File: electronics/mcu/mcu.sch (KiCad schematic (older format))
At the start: 11 parts

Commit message: add footprints
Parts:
- removed X?: 8MHz, symbol CRYSTAL
- added X1: 8MHz, symbol CRYSTAL_S
- C1, C3, C4: renamed from C?; footprint (none) -> Capacitors_ThroughHole:Capacitor7.5MMDiscRM5
- C2: renamed from C?; footprint (none) -> Capacitors_Elko_ThroughHole:Elko_vert_20x10mm_RM5
- IC1: renamed from IC?; footprint SO20 -> SMD_Packages:SO-20-L
- P1: renamed from P?; footprint (none) -> Pin_Headers:Pin_Header_Straight_1x02
- P2: renamed from P?; footprint (none) -> Pin_Headers:Pin_Header_Straight_1x06
- P3: renamed from P?; footprint (none) -> Pin_Headers:Pin_Header_Straight_1x05
- P4: renamed from P?; footprint (none) -> Pin_Headers:Pin_Header_Straight_2x07
- R1: renamed from R?; footprint (none) -> Resistors_ThroughHole:Resistor_Horizontal_RM10mm
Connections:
- wire segments 46 -> 47
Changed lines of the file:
@@
 LIBS:contrib
 LIBS:valves
+LIBS:crystal_s
 LIBS:mcu-cache
 EELAYER 25 0
@@
 $EndDescr
 $Comp
-L ATTINY2313-S IC?
+L ATTINY2313-S IC1
 U 1 1 560C33C8
 P 4900 3300
-F 0 "IC?" H 3950 4300 40  0000 C CNN
+F 0 "IC1" H 3950 4300 40  0000 C CNN
 F 1 "ATTINY2313-S" H 5650 2400 40  0000 C CNN
-F 2 "SO20" H 4900 3300 35  0000 C CIN
+F 2 "SMD_Packages:SO-20-L" H 4900 3300 35  0000 C CIN
 F 3 "" H 4900 3300 60  0000 C CNN
 	1    4900 3300
@@
 $EndComp
 $Comp
-L CONN_01X05 P?
+L CONN_01X05 P3
 U 1 1 560C3E46
 P 7050 3100
-F 0 "P?" H 7050 3400 50  0000 C CNN
+F 0 "P3" H 7050 3400 50  0000 C CNN
 F 1 "SPI" V 7150 3100 50  0000 C CNN
-F 2 "" H 7050 3100 60  0000 C CNN
+F 2 "Pin_Headers:Pin_Header_Straight_1x05" H 7050 3100 60  0001 C CNN
 F 3 "" H 7050 3100 60  0000 C CNN
 	1    7050 3100
@@
 $EndComp
 $Comp
-L GND #PWR?
+L GND #PWR01
 U 1 1 560C404C
 P 6800 3300
-F 0 "#PWR?" H 6800 3050 60  0001 C CNN
+F 0 "#PWR01" H 6800 3050 60  0001 C CNN
 F 1 "GND" H 6800 3150 60  0001 C CNN
 F 2 "" H 6800 3300 60  0000 C CNN
@@
 $EndComp
 $Comp
-L CONN_01X06 P?
+L CONN_01X06 P2
 U 1 1 560C60F9
 P 6400 2650
-F 0 "P?" H 6400 3000 50  0000 C CNN
+F 0 "P2" H 6400 3000 50  0000 C CNN
 F 1 "CONTROL" V 6500 2650 50  0000 C CNN
-F 2 "" H 6400 2650 60  0000 C CNN
+F 2 "Pin_Headers:Pin_Header_Straight_1x06" H 6400 2650 60  0001 C CNN
 F 3 "" H 6400 2650 60  0000 C CNN
 	1    6400 2650
@@
 $EndComp
 $Comp
-L GND #PWR?
+L GND #PWR02
 U 1 1 560C61BB
 P 6150 2400
-F 0 "#PWR?" H 6150 2150 60  0001 C CNN
+F 0 "#PWR02" H 6150 2150 60  0001 C CNN
 F 1 "GND" H 6150 2250 60  0001 C CNN
 F 2 "" H 6150 2400 60  0000 C CNN
@@
 $EndComp
 $Comp
-L CONN_02X07 P?
+L CONN_02X07 P4
 U 1 1 560C626E
 P 6400 3700
-F 0 "P?" H 6400 4100 50  0000 C CNN
+F 0 "P4" H 6400 4100 50  0000 C CNN
 F 1 "EXTRA" V 6400 3700 50  0000 C CNN
-F 2 "" H 6400 2500 60  0000 C CNN
+F 2 "Pin_Headers:Pin_Header_Straight_2x07" H 6400 2500 60  0001 C CNN
 F 3 "" H 6400 2500 60  0000 C CNN
 	1    6400 3700
@@
 $EndComp
 $Comp
-L GND #PWR?
+L GND #PWR03
 U 1 1 560C6457
 P 6750 4100
-F 0 "#PWR?" H 6750 3850 60  0001 C CNN
+F 0 "#PWR03" H 6750 3850 60  0001 C CNN
 F 1 "GND" H 6750 3950 60  0001 C CNN
 F 2 "" H 6750 4100 60  0000 C CNN
@@
 $EndComp
 $Comp
-L GND #PWR?
+L GND #PWR04
 U 1 1 560C656B
 P 4900 4400
-F 0 "#PWR?" H 4900 4150 60  0001 C CNN
+F 0 "#PWR04" H 4900 4150 60  0001 C CNN
 F 1 "GND" H 4900 4250 60  0001 C CNN
 F 2 "" H 4900 4400 60  0000 C CNN
@@
 $EndComp
 $Comp
-L C C?
+L C C4
 U 1 1 560C6654
 P 3650 3400
-F 0 "C?" H 3650 3500 40  0000 L CNN
+F 0 "C4" H 3650 3500 40  0000 L CNN
 F 1 "22p" H 3656 3315 40  0000 L CNN
-F 2 "" H 3688 3250 30  0000 C CNN
+F 2 "Capacitors_ThroughHole:Capacitor7.5MMDiscRM5" H 3688 3250 30  0001 C CNN
 F 3 "" H 3650 3400 60  0000 C CNN
 	1    3650 3400
@@
 $EndComp
 $Comp
-L C C?
+L C C3
 U 1 1 560C6706
 P 2850 3400
-F 0 "C?" H 2850 3500 40  0000 L CNN
+F 0 "C3" H 2850 3500 40  0000 L CNN
 F 1 "22p" H 2856 3315 40  0000 L CNN
-F 2 "" H 2888 3250 30  0000 C CNN
+F 2 "Capacitors_ThroughHole:Capacitor7.5MMDiscRM5" H 2888 3250 30  0001 C CNN
 F 3 "" H 2850 3400 60  0000 C CNN
 	1    2850 3400
 	1    0    0    -1
 $EndComp
-$Comp
-L CRYSTAL X?
-U 1 1 560C6750
-P 3250 3000
-F 0 "X?" H 3250 3150 60  0000 C CNN
-F 1 "8MHz" H 3250 2850 60  0000 C CNN
-F 2 "" H 3250 3000 60  0000 C CNN
-F 3 "" H 3250 3000 60  0000 C CNN
-	1    3250 3000
-	1    0    0    -1
-$EndComp
 Wire Wire Line
 	6850 3200 6050 3200
@@
 Connection ~ 2850 3000
 $Comp
-L GND #PWR?
+L GND #PWR05
 U 1 1 560C6999
 P 3650 3700
-F 0 "#PWR?" H 3650 3450 60  0001 C CNN
+F 0 "#PWR05" H 3650 3450 60  0001 C CNN
 F 1 "GND" H 3650 3550 60  0001 C CNN
 F 2 "" H 3650 3700 60  0000 C CNN
@@
 	3650 3700 3650 3600
 $Comp
-L GND #PWR?
+L GND #PWR06
 U 1 1 560C69EE
 P 2850 3700
-F 0 "#PWR?" H 2850 3450 60  0001 C CNN
+F 0 "#PWR06" H 2850 3450 60  0001 C CNN
 F 1 "GND" H 2850 3550 60  0001 C CNN
 F 2 "" H 2850 3700 60  0000 C CNN
@@
 	2850 3700 2850 3600
 $Comp
-L R R?
+L R R1
 U 1 1 560C6A62
 P 3600 1750
-F 0 "R?" H 3700 1750 40  0000 C CNN
+F 0 "R1" H 3700 1750 40  0000 C CNN
 F 1 "10k" H 3700 1550 40  0000 C CNN
-F 2 "" V 3530 1750 30  0000 C CNN
+F 2 "Resistors_ThroughHole:Resistor_Horizontal_RM10mm" V 3530 1750 30  0001 C CNN
 F 3 "" H 3600 1750 30  0000 C CNN
 	1    3600 1750
@@
 Connection ~ 3600 2100
 $Comp
-L CP2 C?
+L CP2 C2
 U 1 1 560C6C7E
 P 5450 1700
-F 0 "C?" H 5450 1800 40  0000 L CNN
+F 0 "C2" H 5450 1800 40  0000 L CNN
 F 1 "22u" H 5456 1615 40  0000 L CNN
-F 2 "" H 5488 1550 30  0000 C CNN
+F 2 "Capacitors_Elko_ThroughHole:Elko_vert_20x10mm_RM5" H 5488 1550 30  0001 C CNN
 F 3 "" H 5450 1700 60  0000 C CNN
 	1    5450 1700
@@
 $EndComp
 $Comp
-L C C?
+L C C1
 U 1 1 560C6D7B
 P 5150 1700
-F 0 "C?" H 5150 1800 40  0000 L CNN
+F 0 "C1" H 5150 1800 40  0000 L CNN
 F 1 "100n" H 5156 1615 40  0000 L CNN
-F 2 "" H 5188 1550 30  0000 C CNN
+F 2 "Capacitors_ThroughHole:Capacitor7.5MMDiscRM5" H 5188 1550 30  0001 C CNN
 F 3 "" H 5150 1700 60  0000 C CNN
 	1    5150 1700
@@
 $EndComp
 $Comp
-L CONN_01X02 P?
+L CONN_01X02 P1
 U 1 1 560C6E13
 P 6050 1450
-F 0 "P?" H 6050 1600 50  0000 C CNN
+F 0 "P1" H 6050 1600 50  0000 C CNN
 F 1 "3.3v" V 6150 1450 50  0000 C CNN
-F 2 "" H 6050 1450 60  0000 C CNN
+F 2 "Pin_Headers:Pin_Header_Straight_1x02" H 6050 1450 60  0001 C CNN
 F 3 "" H 6050 1450 60  0000 C CNN
 	1    6050 1450
@@
 Connection ~ 5450 1400
 $Comp
-L GND #PWR?
+L GND #PWR07
 U 1 1 560C6FBB
 P 5150 1950
-F 0 "#PWR?" H 5150 1700 60  0001 C CNN
+F 0 "#PWR07" H 5150 1700 60  0001 C CNN
 F 1 "GND" H 5150 1800 60  0001 C CNN
 F 2 "" H 5150 1950 60  0000 C CNN
@@
 	5150 1950 5150 1900
 $Comp
-L GND #PWR?
+L GND #PWR08
 U 1 1 560C7062
 P 5450 1950
-F 0 "#PWR?" H 5450 1700 60  0001 C CNN
+F 0 "#PWR08" H 5450 1700 60  0001 C CNN
 F 1 "GND" H 5450 1800 60  0001 C CNN
 F 2 "" H 5450 1950 60  0000 C CNN
@@
 	5450 1950 5450 1900
 $Comp
-L GND #PWR?
+L GND #PWR09
 U 1 1 560C70E9
 P 5800 1500
-F 0 "#PWR?" H 5800 1250 60  0001 C CNN
+F 0 "#PWR09" H 5800 1250 60  0001 C CNN
 F 1 "GND" H 5800 1350 60  0001 C CNN
 F 2 "" H 5800 1500 60  0000 C CNN
@@
 Wire Wire Line
 	5850 1500 5800 1500
+$Comp
+L CRYSTAL_S X1
+U 1 1 560C845C
+P 3250 3000
+F 0 "X1" H 3250 3150 60  0000 C CNN
+F 1 "8MHz" H 3400 2800 60  0000 C CNN
+F 2 "" H 3250 3000 60  0000 C CNN
+F 3 "" H 3250 3000 60  0000 C CNN
+	1    3250 3000
+	1    0    0    -1
+$EndComp
+$Comp
+L GND #PWR?
+U 1 1 560C8672
+P 3250 3350
+F 0 "#PWR?" H 3250 3100 60  0001 C CNN
+F 1 "GND" H 3250 3200 60  0001 C CNN
+F 2 "" H 3250 3350 60  0000 C CNN
+F 3 "" H 3250 3350 60  0000 C CNN
+	1    3250 3350
+	1    0    0    -1
+$EndComp
+Wire Wire Line
+	3250 3350 3250 3250
 $EndSCHEMATC

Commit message: some minor tweaks
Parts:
- X1: footprint (none) -> QMONTRE_P:QMONTRE_P
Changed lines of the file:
@@
 F 0 "X1" H 3250 3150 60  0000 C CNN
 F 1 "8MHz" H 3400 2800 60  0000 C CNN
-F 2 "" H 3250 3000 60  0000 C CNN
+F 2 "QMONTRE_P:QMONTRE_P" H 3250 3000 60  0001 C CNN
 F 3 "" H 3250 3000 60  0000 C CNN
 	1    3250 3000
@@
 $EndComp
 $Comp
-L GND #PWR?
+L GND #PWR010
 U 1 1 560C8672
 P 3250 3350
-F 0 "#PWR?" H 3250 3100 60  0001 C CNN
+F 0 "#PWR010" H 3250 3100 60  0001 C CNN
 F 1 "GND" H 3250 3200 60  0001 C CNN
 F 2 "" H 3250 3350 60  0000 C CNN

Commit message: finish the pcb
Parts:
- removed P4: EXTRA, Pin_Headers:Pin_Header_Straight_2x07, symbol CONN_02X07
- added P4: EXTRA, symbol CONN_02X06
- X1: footprint QMONTRE_P:QMONTRE_P -> HC-49V_S:HC-49V_S
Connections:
- net GND: now also P4.10 (P10), P4.12 (P12), P4.2 (P2), P4.4 (P4), P4.6 (P6), P4.8 (P8)
- net at IC1.2 ((RXD)PD0): now also P4.1 (P1)
- net at IC1.3 ((TXD)PD1): now also P4.3 (P3)
- net at IC1.6 ((CKOUT/XCK/INT0)PD2): now also P4.5 (P5)
- net at IC1.7 ((INT1)PD3): now also P4.7 (P7)
- net at IC1.8 ((T0)PD4): now also P4.9 (P9)
- net at IC1.9 ((OC0B/T1)PD5): now also P4.11 (P11)
- no-connect marks 0 -> 1
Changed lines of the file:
@@
 $EndComp
 $Comp
-L GND #PWR01
+L GND #PWR5
 U 1 1 560C404C
 P 6800 3300
-F 0 "#PWR01" H 6800 3050 60  0001 C CNN
+F 0 "#PWR5" H 6800 3050 60  0001 C CNN
 F 1 "GND" H 6800 3150 60  0001 C CNN
 F 2 "" H 6800 3300 60  0000 C CNN
@@
 $EndComp
 $Comp
-L GND #PWR02
+L GND #PWR4
 U 1 1 560C61BB
 P 6150 2400
-F 0 "#PWR02" H 6150 2150 60  0001 C CNN
+F 0 "#PWR4" H 6150 2150 60  0001 C CNN
 F 1 "GND" H 6150 2250 60  0001 C CNN
 F 2 "" H 6150 2400 60  0000 C CNN
@@
 $EndComp
 $Comp
-L CONN_02X07 P4
-U 1 1 560C626E
-P 6400 3700
-F 0 "P4" H 6400 4100 50  0000 C CNN
-F 1 "EXTRA" V 6400 3700 50  0000 C CNN
-F 2 "Pin_Headers:Pin_Header_Straight_2x07" H 6400 2500 60  0001 C CNN
-F 3 "" H 6400 2500 60  0000 C CNN
-	1    6400 3700
-	1    0    0    -1
-$EndComp
-$Comp
-L GND #PWR03
+L GND #PWR9
 U 1 1 560C6457
 P 6750 4100
-F 0 "#PWR03" H 6750 3850 60  0001 C CNN
+F 0 "#PWR9" H 6750 3850 60  0001 C CNN
 F 1 "GND" H 6750 3950 60  0001 C CNN
 F 2 "" H 6750 4100 60  0000 C CNN
@@
 $EndComp
 $Comp
-L GND #PWR04
+L GND #PWR10
 U 1 1 560C656B
 P 4900 4400
-F 0 "#PWR04" H 4900 4150 60  0001 C CNN
+F 0 "#PWR10" H 4900 4150 60  0001 C CNN
 F 1 "GND" H 4900 4250 60  0001 C CNN
 F 2 "" H 4900 4400 60  0000 C CNN
@@
 	6050 3900 6150 3900
 Wire Wire Line
-	6150 4000 6050 4000
-Wire Wire Line
 	6750 4100 6750 3400
 Wire Wire Line
@@
 Connection ~ 6750 3900
 Wire Wire Line
-	6650 4000 6750 4000
-Connection ~ 6750 4000
-Wire Wire Line
 	4900 4400 4900 4300
 Wire Wire Line
@@
 Connection ~ 2850 3000
 $Comp
-L GND #PWR05
+L GND #PWR8
 U 1 1 560C6999
 P 3650 3700
-F 0 "#PWR05" H 3650 3450 60  0001 C CNN
+F 0 "#PWR8" H 3650 3450 60  0001 C CNN
 F 1 "GND" H 3650 3550 60  0001 C CNN
 F 2 "" H 3650 3700 60  0000 C CNN
@@
 	3650 3700 3650 3600
 $Comp
-L GND #PWR06
+L GND #PWR7
 U 1 1 560C69EE
 P 2850 3700
-F 0 "#PWR06" H 2850 3450 60  0001 C CNN
+F 0 "#PWR7" H 2850 3450 60  0001 C CNN
 F 1 "GND" H 2850 3550 60  0001 C CNN
 F 2 "" H 2850 3700 60  0000 C CNN
@@
 Connection ~ 5450 1400
 $Comp
-L GND #PWR07
+L GND #PWR2
 U 1 1 560C6FBB
 P 5150 1950
-F 0 "#PWR07" H 5150 1700 60  0001 C CNN
+F 0 "#PWR2" H 5150 1700 60  0001 C CNN
 F 1 "GND" H 5150 1800 60  0001 C CNN
 F 2 "" H 5150 1950 60  0000 C CNN
@@
 	5150 1950 5150 1900
 $Comp
-L GND #PWR08
+L GND #PWR3
 U 1 1 560C7062
 P 5450 1950
-F 0 "#PWR08" H 5450 1700 60  0001 C CNN
+F 0 "#PWR3" H 5450 1700 60  0001 C CNN
 F 1 "GND" H 5450 1800 60  0001 C CNN
 F 2 "" H 5450 1950 60  0000 C CNN
@@
 	5450 1950 5450 1900
 $Comp
-L GND #PWR09
+L GND #PWR1
 U 1 1 560C70E9
 P 5800 1500
-F 0 "#PWR09" H 5800 1250 60  0001 C CNN
+F 0 "#PWR1" H 5800 1250 60  0001 C CNN
 F 1 "GND" H 5800 1350 60  0001 C CNN
 F 2 "" H 5800 1500 60  0000 C CNN
@@
 F 0 "X1" H 3250 3150 60  0000 C CNN
 F 1 "8MHz" H 3400 2800 60  0000 C CNN
-F 2 "QMONTRE_P:QMONTRE_P" H 3250 3000 60  0001 C CNN
+F 2 "HC-49V_S:HC-49V_S" H 3250 3000 60  0001 C CNN
 F 3 "" H 3250 3000 60  0000 C CNN
 	1    3250 3000
@@
 $EndComp
 $Comp
-L GND #PWR010
+L GND #PWR6
 U 1 1 560C8672
 P 3250 3350
-F 0 "#PWR010" H 3250 3100 60  0001 C CNN
+F 0 "#PWR6" H 3250 3100 60  0001 C CNN
 F 1 "GND" H 3250 3200 60  0001 C CNN
 F 2 "" H 3250 3350 60  0000 C CNN
@@
 Wire Wire Line
 	3250 3350 3250 3250
+$Comp
+L CONN_02X06 P4
+U 1 1 561BC094
+P 6400 3650
+F 0 "P4" H 6400 4000 50  0000 C CNN
+F 1 "EXTRA" V 6400 3650 50  0000 C CNN
+F 2 "" H 6400 2450 60  0000 C CNN
+F 3 "" H 6400 2450 60  0000 C CNN
+	1    6400 3650
+	1    0    0    -1
+$EndComp
+NoConn ~ 6050 4000
 $EndSCHEMATC

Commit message: finish the PCB
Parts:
- P4: footprint (none) -> Pin_Headers:Pin_Header_Straight_2x06
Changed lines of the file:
@@
 $EndComp
 $Comp
-L GND #PWR5
+L GND #PWR01
 U 1 1 560C404C
 P 6800 3300
-F 0 "#PWR5" H 6800 3050 60  0001 C CNN
+F 0 "#PWR01" H 6800 3050 60  0001 C CNN
 F 1 "GND" H 6800 3150 60  0001 C CNN
 F 2 "" H 6800 3300 60  0000 C CNN
@@
 $EndComp
 $Comp
-L GND #PWR4
+L GND #PWR02
 U 1 1 560C61BB
 P 6150 2400
-F 0 "#PWR4" H 6150 2150 60  0001 C CNN
+F 0 "#PWR02" H 6150 2150 60  0001 C CNN
 F 1 "GND" H 6150 2250 60  0001 C CNN
 F 2 "" H 6150 2400 60  0000 C CNN
@@
 $EndComp
 $Comp
-L GND #PWR9
+L GND #PWR03
 U 1 1 560C6457
 P 6750 4100
-F 0 "#PWR9" H 6750 3850 60  0001 C CNN
+F 0 "#PWR03" H 6750 3850 60  0001 C CNN
 F 1 "GND" H 6750 3950 60  0001 C CNN
 F 2 "" H 6750 4100 60  0000 C CNN
@@
 $EndComp
 $Comp
-L GND #PWR10
+L GND #PWR04
 U 1 1 560C656B
 P 4900 4400
-F 0 "#PWR10" H 4900 4150 60  0001 C CNN
+F 0 "#PWR04" H 4900 4150 60  0001 C CNN
 F 1 "GND" H 4900 4250 60  0001 C CNN
 F 2 "" H 4900 4400 60  0000 C CNN
@@
 Connection ~ 2850 3000
 $Comp
-L GND #PWR8
+L GND #PWR05
 U 1 1 560C6999
 P 3650 3700
-F 0 "#PWR8" H 3650 3450 60  0001 C CNN
+F 0 "#PWR05" H 3650 3450 60  0001 C CNN
 F 1 "GND" H 3650 3550 60  0001 C CNN
 F 2 "" H 3650 3700 60  0000 C CNN
@@
 	3650 3700 3650 3600
 $Comp
-L GND #PWR7
+L GND #PWR06
 U 1 1 560C69EE
 P 2850 3700
-F 0 "#PWR7" H 2850 3450 60  0001 C CNN
+F 0 "#PWR06" H 2850 3450 60  0001 C CNN
 F 1 "GND" H 2850 3550 60  0001 C CNN
 F 2 "" H 2850 3700 60  0000 C CNN
@@
 Connection ~ 5450 1400
 $Comp
-L GND #PWR2
+L GND #PWR07
 U 1 1 560C6FBB
 P 5150 1950
-F 0 "#PWR2" H 5150 1700 60  0001 C CNN
+F 0 "#PWR07" H 5150 1700 60  0001 C CNN
 F 1 "GND" H 5150 1800 60  0001 C CNN
 F 2 "" H 5150 1950 60  0000 C CNN
@@
 	5150 1950 5150 1900
 $Comp
-L GND #PWR3
+L GND #PWR08
 U 1 1 560C7062
 P 5450 1950
-F 0 "#PWR3" H 5450 1700 60  0001 C CNN
+F 0 "#PWR08" H 5450 1700 60  0001 C CNN
 F 1 "GND" H 5450 1800 60  0001 C CNN
 F 2 "" H 5450 1950 60  0000 C CNN
@@
 	5450 1950 5450 1900
 $Comp
-L GND #PWR1
+L GND #PWR09
 U 1 1 560C70E9
 P 5800 1500
-F 0 "#PWR1" H 5800 1250 60  0001 C CNN
+F 0 "#PWR09" H 5800 1250 60  0001 C CNN
 F 1 "GND" H 5800 1350 60  0001 C CNN
 F 2 "" H 5800 1500 60  0000 C CNN
@@
 $EndComp
 $Comp
-L GND #PWR6
+L GND #PWR010
 U 1 1 560C8672
 P 3250 3350
-F 0 "#PWR6" H 3250 3100 60  0001 C CNN
+F 0 "#PWR010" H 3250 3100 60  0001 C CNN
 F 1 "GND" H 3250 3200 60  0001 C CNN
 F 2 "" H 3250 3350 60  0000 C CNN
@@
 F 0 "P4" H 6400 4000 50  0000 C CNN
 F 1 "EXTRA" V 6400 3650 50  0000 C CNN
-F 2 "" H 6400 2450 60  0000 C CNN
+F 2 "Pin_Headers:Pin_Header_Straight_2x06" H 6400 2450 60  0001 C CNN
 F 3 "" H 6400 2450 60  0000 C CNN
 	1    6400 3650

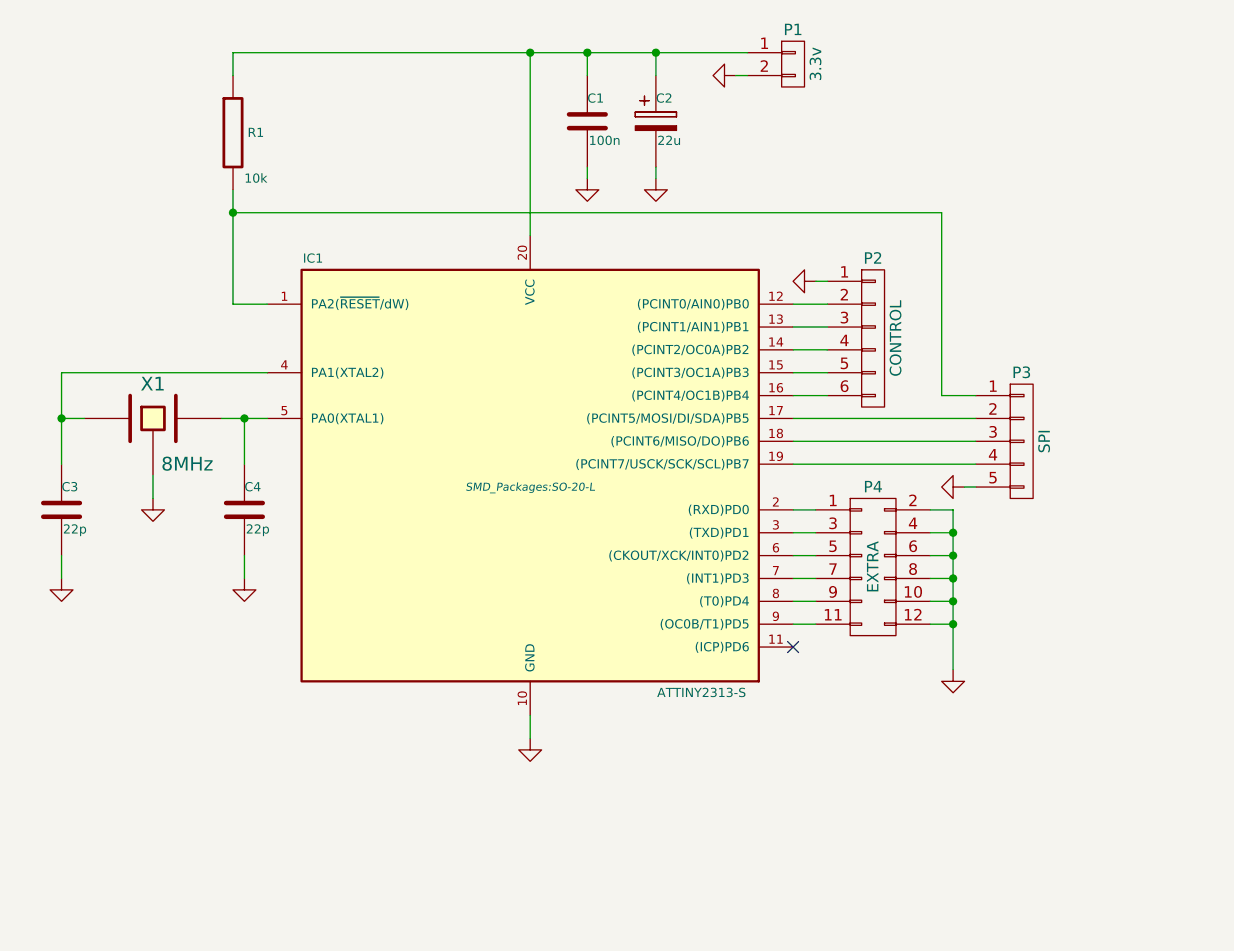
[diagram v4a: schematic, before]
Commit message: join uart and spi on the mcu pcb
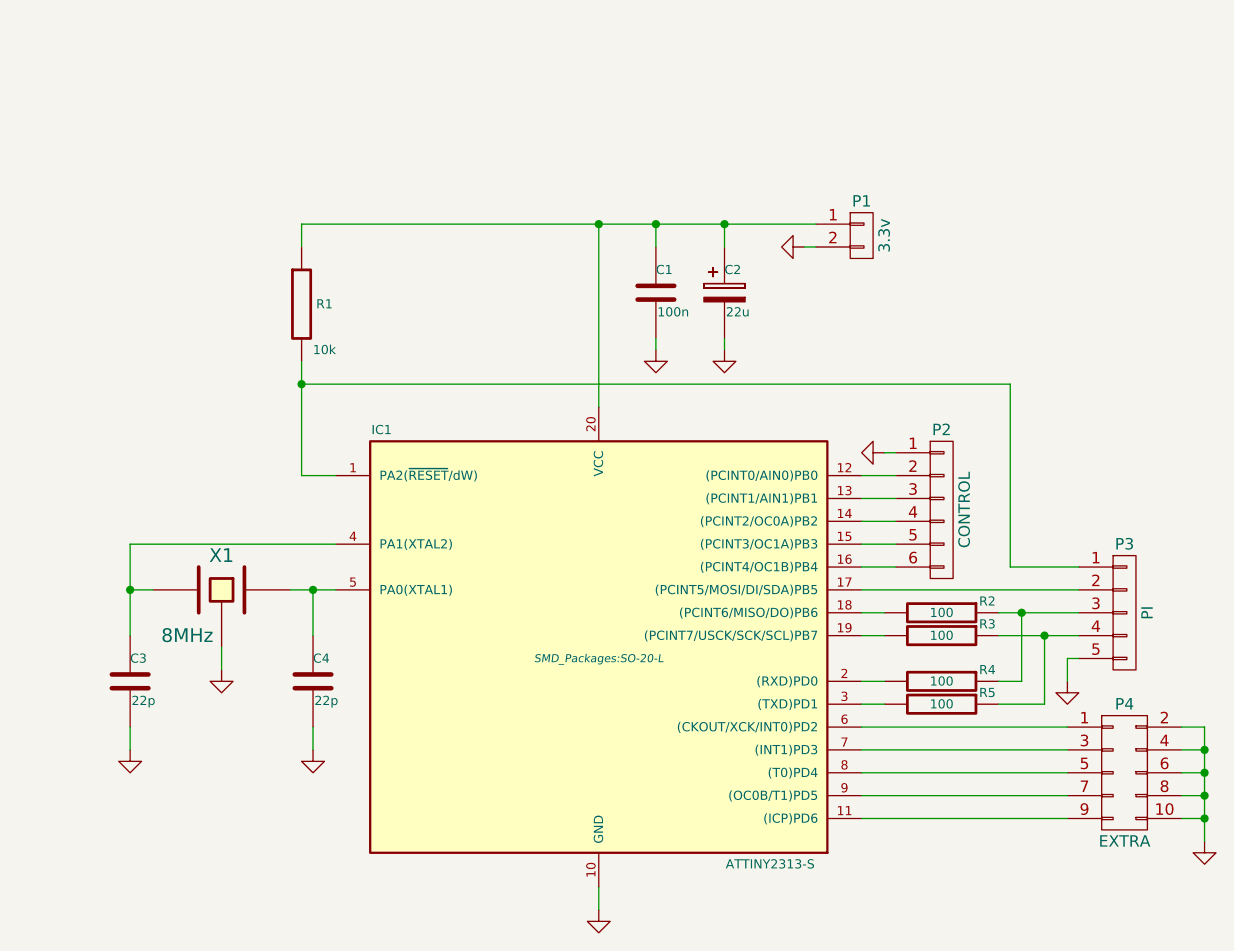
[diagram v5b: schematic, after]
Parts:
- removed P4: EXTRA, Pin_Headers:Pin_Header_Straight_2x06, symbol CONN_02X06
- added P4: EXTRA, Pin_Headers:Pin_Header_Straight_2x05, symbol CONN_02X05
- added R2, R3, R4, R5: 100, Resistors_SMD:R_0805, symbol R
- P3: value SPI -> PI
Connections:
- net GND: now also P4.10 (P10), P4.2 (P2), P4.4 (P4), P4.6 (P6), P4.8 (P8)
- net at IC1.11 ((ICP)PD6): now also P4.9 (P9)
- net at IC1.18 ((PCINT6/MISO/DO)PB6): now also R2.2; no longer P3.3 (P3)
- net at IC1.19 ((PCINT7/USCK/SCK/SCL)PB7): now also R3.2; no longer P3.4 (P4)
- net at IC1.2 ((RXD)PD0): now also R4.2
- net at IC1.3 ((TXD)PD1): now also R5.2
- net at C3.1, IC1.4 (PA1(XTAL2)): now also X1.2; no longer X1.1
- net at C4.1, IC1.5 (PA0(XTAL1)): now also X1.1; no longer X1.2
- net at IC1.6 ((CKOUT/XCK/INT0)PD2): now also P4.1 (P1)
- net at IC1.7 ((INT1)PD3): now also P4.3 (P3)
- net at IC1.8 ((T0)PD4): now also P4.5 (P5)
- net at IC1.9 ((OC0B/T1)PD5): now also P4.7 (P7)
- new net: P3.3 (P3), R2.1, R4.1
- new net: P3.4 (P4), R3.1, R5.1
- no-connect marks 1 -> 0
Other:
- moved on the sheet: C1, C2, C3, C4, IC1, P1, P2, P3, R1, X1
